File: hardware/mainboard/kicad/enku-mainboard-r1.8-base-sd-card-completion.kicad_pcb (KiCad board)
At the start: 4 copper layers, 59 x 101 mm, 132 parts, among them J1 1S LiPo + NTC, J2 Hirose DM3AT-SF-PEJM5, J3 FH34SRJ-24S-0.5SH(50), J5 GCT USB4105-GF-A-120, J6 4-pin pogo dock, J7 Tag-Connect TC2030-IDC-NL, Q1 IRLML6346TRPBF, Q2 AO3401A, SW1 HARD POWER, SW2 BOOT / RECOVERY, SW3 BTN_L1, SW4 BTN_L2, SW5 BTN_R1, SW6 BTN_R2, U1 ESP32-S3-WROOM-1-N16R8, U10 TLV3012BIDBVR, U2 TPS2121, U3 BQ25185DLHR, U4 TPS63802DLAR, U5 BMI270, U8 USBLC6-2SC6, U9 TMUX1101DBVR

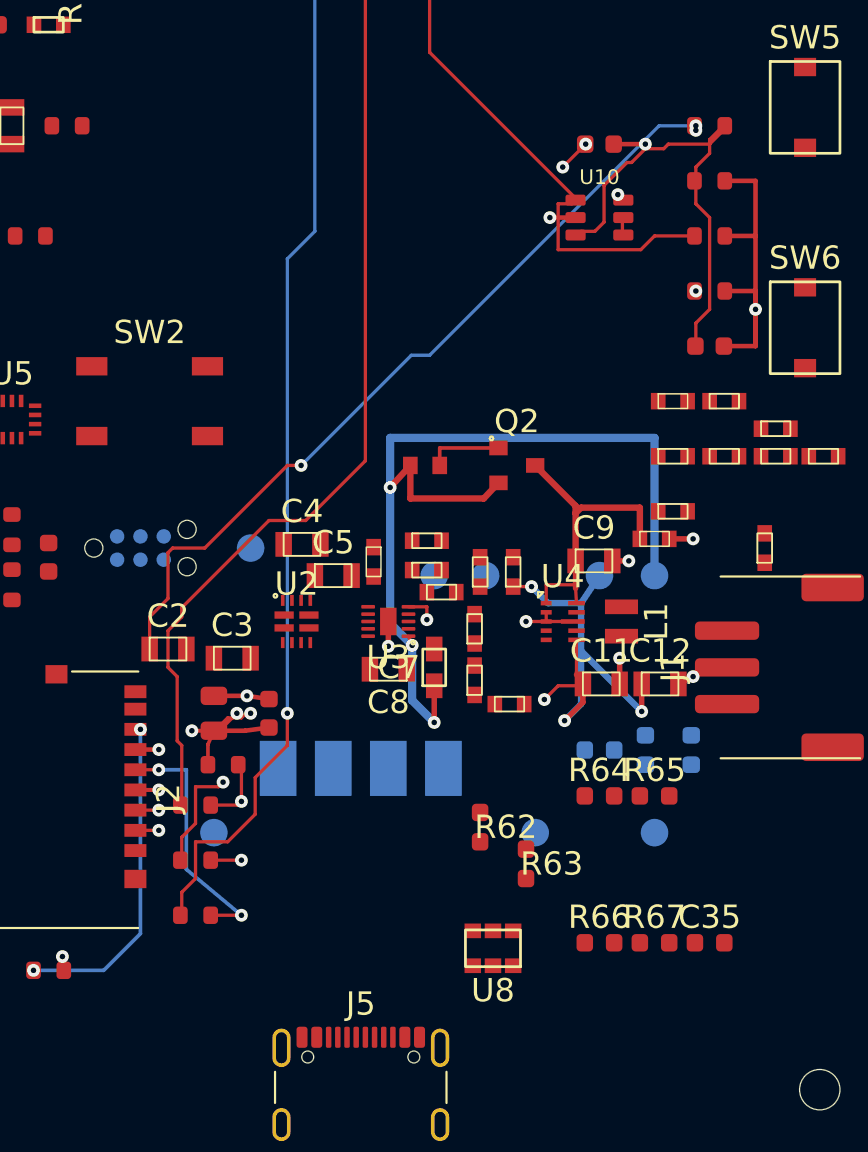
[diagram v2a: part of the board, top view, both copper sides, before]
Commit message: R41: correct ST ESD lands and route USB CC/VBUS power; fix GND clearances
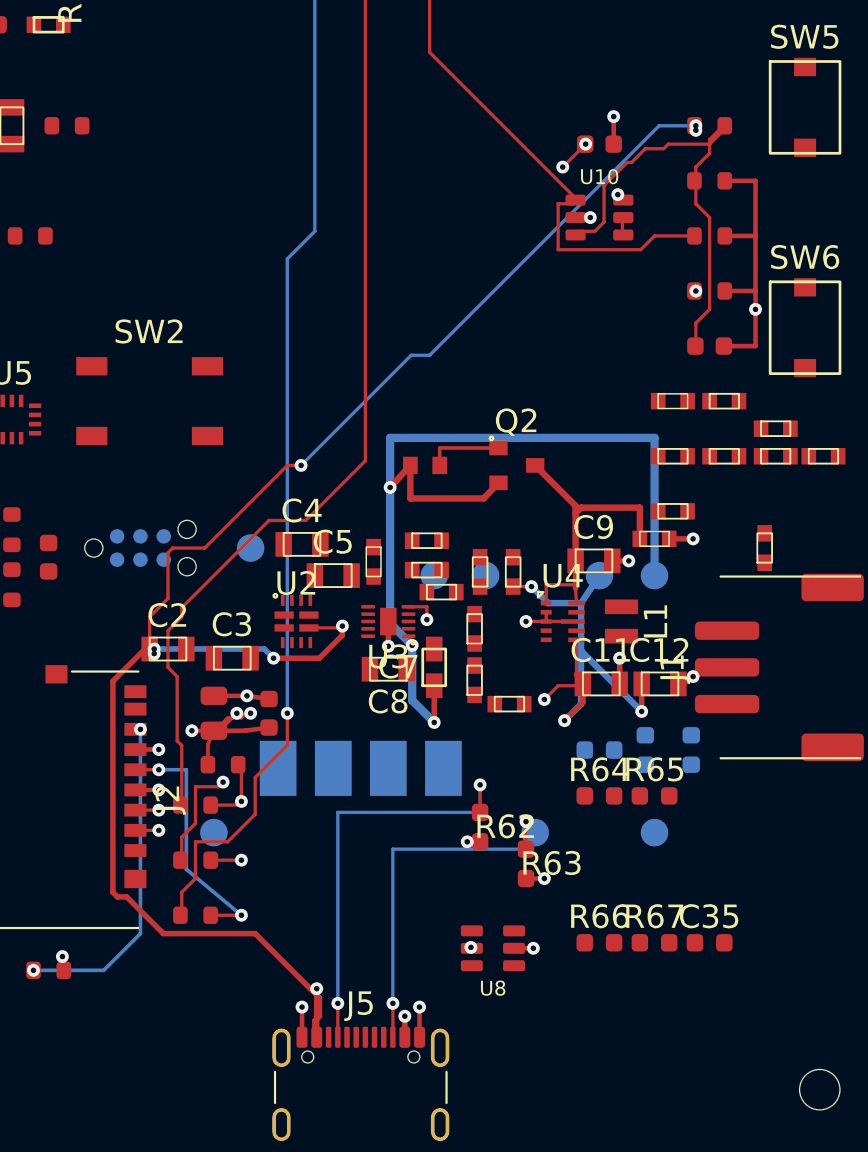
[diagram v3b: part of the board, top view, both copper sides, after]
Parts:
- U8: footprint Package_TO_SOT_SMD:SOT-23-6 -> ENKU:USBLC6_2SC6_ST_SOT23_6L
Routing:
- net VBUS_USB: track 53.0 -> 134.0 mm, vias 4 -> 11
- net USB_CC1: track 0.00 -> 23.0 mm, vias 0 -> 2
- net USB_CC2: track 0.00 -> 20.5 mm, vias 0 -> 2
- net GND: track 43.0 -> 45.2 mm, vias 15 -> 20
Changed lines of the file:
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@@
     (pad "S" thru_hole oval (at 4.32 1.075) (size 1 1.8) (drill oval 0.6 1.4) (layers "*.Cu" "*.Mask") (net 8 "USB_SHIELD"))
   )
-  (footprint "Package_TO_SOT_SMD:SOT-23-6" (layer "F.Cu")
-    (at 54.2 108.8 180)
-    (property "Reference" "U8" (at 0 -2.3 0) (layer "F.SilkS"))
-    (property "Value" "USBLC6-2SC6" (at 0 2.3 0) (layer "F.Fab") hide)
-    (fp_rect (start -1.5 -1) (end 1.5 1)
-      (stroke (width 0.15) (type default)) (fill none) (layer "F.SilkS"))
-    (pad "1" smd rect (at -1.1 -0.95) (size 0.9 0.8) (layers "F.Cu" "F.Paste" "F.Mask") (net 6 "USB_DP_CONN"))
-    (pad "2" smd rect (at 0 -0.95) (size 0.9 0.8) (layers "F.Cu" "F.Paste" "F.Mask") (net 1 "GND"))
-    (pad "3" smd rect (at 1.1 -0.95) (size 0.9 0.8) (layers "F.Cu" "F.Paste" "F.Mask") (net 7 "USB_DM_CONN"))
-    (pad "4" smd rect (at 1.1 0.95) (size 0.9 0.8) (layers "F.Cu" "F.Paste" "F.Mask") (net 7 "USB_DM_CONN"))
-    (pad "5" smd rect (at 0 0.95) (size 0.9 0.8) (layers "F.Cu" "F.Paste" "F.Mask") (net 3 "VBUS_USB"))
-    (pad "6" smd rect (at -1.1 0.95) (size 0.9 0.8) (layers "F.Cu" "F.Paste" "F.Mask") (net 6 "USB_DP_CONN"))
-  )
+  (footprint "ENKU:USBLC6_2SC6_ST_SOT23_6L" (layer "F.Cu") (at 54.2 108.8 180) (attr smd)
+(property "Reference" "U8" (at 0 -2.2) (layer "F.SilkS") (effects (font (size 0.8 0.8) (thickness 0.12))))
+(property "Value" "USBLC6-2SC6" (at 0 2.2) (layer "F.Fab") (effects (font (size 0.8 0.8) (thickness 0.12))))
+(fp_rect (start -0.8 -1.5) (end 0.8 1.5) (stroke (width 0.1) (type default)) (fill none) (layer "F.Fab"))
+(fp_rect (start -2 -1.75) (end 2 1.75) (stroke (width 0.05) (type default)) (fill none) (layer "F.CrtYd"))
+(pad "1" smd roundrect (at -1.15 -0.95) (size 1.2 0.6) (layers "F.Cu" "F.Paste" "F.Mask") (roundrect_rratio 0.2) (net 6 "USB_DP_CONN"))
+(pad "2" smd roundrect (at -1.15 0) (size 1.2 0.6) (layers "F.Cu" "F.Paste" "F.Mask") (roundrect_rratio 0.2) (net 1 "GND"))
+(pad "3" smd roundrect (at -1.15 0.95) (size 1.2 0.6) (layers "F.Cu" "F.Paste" "F.Mask") (roundrect_rratio 0.2) (net 7 "USB_DM_CONN"))
+(pad "4" smd roundrect (at 1.15 0.95) (size 1.2 0.6) (layers "F.Cu" "F.Paste" "F.Mask") (roundrect_rratio 0.2) (net 7 "USB_DM_CONN"))
+(pad "5" smd roundrect (at 1.15 0) (size 1.2 0.6) (layers "F.Cu" "F.Paste" "F.Mask") (roundrect_rratio 0.2) (net 3 "VBUS_USB"))
+(pad "6" smd roundrect (at 1.15 -0.95) (size 1.2 0.6) (layers "F.Cu" "F.Paste" "F.Mask") (roundrect_rratio 0.2) (net 6 "USB_DP_CONN"))
+)
   (footprint "ENKU:HARD_POWER_SWITCH_PLACEMENT" (layer "F.Cu")
     (at 30.5 29)
@@
     (min_thickness 0.25)
     (fill yes (thermal_gap 0.30) (thermal_bridge_width 0.30))
-    (polygon (pts (xy 27 35) (xy 69 35) (xy 69 111) (xy 27 111)))
+    (polygon (pts (xy 27 35) (xy 69 35) (xy 69 119) (xy 27 119)))
   )
   (segment (start 39 95.05) (end 40.8 95.05) (width 0.25) (layer "F.Cu") (net 1))
@@
     (min_thickness 0.25)
     (fill yes (thermal_gap 0.30) (thermal_bridge_width 0.30))
-    (polygon (pts (xy 27 35) (xy 69 35) (xy 69 111) (xy 27 111)))
+    (polygon (pts (xy 27 35) (xy 69 35) (xy 69 119) (xy 27 119)))
   )
   (segment (start 27.74 53.75) (end 27.74 55.5) (width 0.25) (layer "F.Cu") (net 1))
@@
   (segment (start 35.46 46.5) (end 35.46 49.5) (width 0.25) (layer "F.Cu") (net 1))
   (segment (start 34.725 97.975) (end 36 97.975) (width 0.25) (layer "F.Cu") (net 1))
-  (segment (start 58.7 69) (end 57.3 69) (width 0.25) (layer "F.Cu") (net 1))
-  (segment (start 60.775 65) (end 62.5 65) (width 0.25) (layer "F.Cu") (net 1))
+  (segment (start 58.7 69) (end 59.5 69) (width 0.25) (layer "F.Cu") (net 1))
+  (segment (start 60.775 65) (end 60.775 63.5) (width 0.25) (layer "F.Cu") (net 1))
   (segment (start 66.825 67) (end 68.5 67) (width 0.25) (layer "F.Cu") (net 1))
   (segment (start 68.5 67) (end 68.5 70) (width 0.25) (layer "F.Cu") (net 1))
@@
   (segment (start 68.5 70) (end 68.5 73) (width 0.25) (layer "F.Cu") (net 1))
   (segment (start 68.5 73) (end 66.825 73) (width 0.25) (layer "F.Cu") (net 1))
-  (segment (start 68.5 73) (end 68.5 76) (width 0.25) (layer "F.Cu") (net 1))
   (segment (start 68.5 76) (end 66.775 76) (width 0.25) (layer "F.Cu") (net 1))
   (segment (start 68.5 73) (end 68.5 74) (width 0.25) (layer "F.Cu") (net 1))
@@
   (via (at 35.46 49.5) (size 0.70) (drill 0.30) (layers "F.Cu" "B.Cu") (net 1))
   (via (at 36 97.975) (size 0.70) (drill 0.30) (layers "F.Cu" "B.Cu") (net 1))
-  (via (at 57.3 69) (size 0.70) (drill 0.30) (layers "F.Cu" "B.Cu") (net 1))
-  (via (at 62.5 65) (size 0.70) (drill 0.30) (layers "F.Cu" "B.Cu") (net 1))
+  (via (at 59.5 69) (size 0.70) (drill 0.30) (layers "F.Cu" "B.Cu") (net 1))
+  (via (at 60.775 63.5) (size 0.70) (drill 0.30) (layers "F.Cu" "B.Cu") (net 1))
   (via (at 68.5 74) (size 0.70) (drill 0.30) (layers "F.Cu" "B.Cu") (net 1))
+  (segment (start 45.75 113.645) (end 45.75 111.8) (width 0.18) (layer "F.Cu") (net 4))
+  (segment (start 45.75 111.8) (end 45.75 101.4) (width 0.18) (layer "B.Cu") (net 4))
+  (segment (start 45.75 101.4) (end 53.5 101.4) (width 0.18) (layer "B.Cu") (net 4))
+  (segment (start 53.5 101.4) (end 53.5 99.9) (width 0.18) (layer "B.Cu") (net 4))
+  (segment (start 53.5 99.9) (end 53.5 101.4) (width 0.18) (layer "F.Cu") (net 4))
+  (segment (start 48.75 113.645) (end 48.75 111.8) (width 0.18) (layer "F.Cu") (net 5))
+  (segment (start 48.75 111.8) (end 48.75 103.4) (width 0.18) (layer "B.Cu") (net 5))
+  (segment (start 48.75 103.4) (end 56 103.4) (width 0.18) (layer "B.Cu") (net 5))
+  (segment (start 56 103.4) (end 56 101.9) (width 0.18) (layer "B.Cu") (net 5))
+  (segment (start 56 101.9) (end 56 103.4) (width 0.18) (layer "F.Cu") (net 5))
+  (segment (start 43.8 113.645) (end 43.8 112.0) (width 0.25) (layer "F.Cu") (net 1))
+  (segment (start 50.2 113.645) (end 50.2 112.0) (width 0.25) (layer "F.Cu") (net 1))
+  (segment (start 53.5 103) (end 52.8 103) (width 0.25) (layer "F.Cu") (net 1))
+  (segment (start 56 105) (end 57 105) (width 0.25) (layer "F.Cu") (net 1))
+  (segment (start 55.35 108.8) (end 56.4 108.8) (width 0.25) (layer "F.Cu") (net 1))
+  (via (at 45.75 111.8) (size 0.70) (drill 0.30) (layers "F.Cu" "B.Cu") (net 4))
+  (via (at 53.5 99.9) (size 0.70) (drill 0.30) (layers "F.Cu" "B.Cu") (net 4))
+  (via (at 48.75 111.8) (size 0.70) (drill 0.30) (layers "F.Cu" "B.Cu") (net 5))
+  (via (at 56 101.9) (size 0.70) (drill 0.30) (layers "F.Cu" "B.Cu") (net 5))
+  (via (at 43.8 112.0) (size 0.70) (drill 0.30) (layers "F.Cu" "B.Cu") (net 1))
+  (via (at 50.2 112.0) (size 0.70) (drill 0.30) (layers "F.Cu" "B.Cu") (net 1))
+  (via (at 52.8 103) (size 0.70) (drill 0.30) (layers "F.Cu" "B.Cu") (net 1))
+  (via (at 57 105) (size 0.70) (drill 0.30) (layers "F.Cu" "B.Cu") (net 1))
+  (via (at 56.4 108.8) (size 0.70) (drill 0.30) (layers "F.Cu" "B.Cu") (net 1))
+  (segment (start 44.175 91.35) (end 46 91.35) (width 0.18) (layer "F.Cu") (net 3))
+  (segment (start 46 91.35) (end 46 91.25) (width 0.18) (layer "F.Cu") (net 3))
+  (via (at 46 91.25) (size 0.70) (drill 0.30) (layers "F.Cu" "B.Cu") (net 3))
+  (segment (start 49.4 113.645) (end 49.4 112.5) (width 0.30) (layer "F.Cu") (net 3))
+  (segment (start 44.6 113.645) (end 44.6 111) (width 0.30) (layer "F.Cu") (net 3))
+  (segment (start 49.4 112.5) (end 44.6 112.5) (width 0.30) (layer "In1.Cu") (net 3))
+  (segment (start 44.6 112.5) (end 44.6 111) (width 0.30) (layer "In1.Cu") (net 3))
+  (via (at 49.4 112.5) (size 0.70) (drill 0.30) (layers "F.Cu" "B.Cu") (net 3))
+  (via (at 44.6 111) (size 0.70) (drill 0.30) (layers "F.Cu" "B.Cu") (net 3))
+  (segment (start 44.5 113.75) (end 44.5 112.75) (width 0.30) (layer "F.Cu") (net 3))
+  (segment (start 44.5 112.75) (end 44.75 112.5) (width 0.30) (layer "F.Cu") (net 3))
+  (segment (start 44.75 112.5) (end 44.75 111.5) (width 0.30) (layer "F.Cu") (net 3))
+  (segment (start 44.75 111.5) (end 41.25 108.0) (width 0.30) (layer "F.Cu") (net 3))
+  (segment (start 41.25 108.0) (end 36.25 108.0) (width 0.30) (layer "F.Cu") (net 3))
+  (segment (start 36.25 108.0) (end 34.25 106.0) (width 0.30) (layer "F.Cu") (net 3))
+  (segment (start 34.25 106.0) (end 33.75 106.0) (width 0.30) (layer "F.Cu") (net 3))
+  (segment (start 33.75 106.0) (end 33.5 105.75) (width 0.30) (layer "F.Cu") (net 3))
+  (segment (start 33.5 105.75) (end 33.5 94.25) (width 0.30) (layer "F.Cu") (net 3))
+  (segment (start 33.5 94.25) (end 35.25 92.5) (width 0.30) (layer "F.Cu") (net 3))
+  (segment (start 35.25 92.5) (end 35.5 92.5) (width 0.30) (layer "F.Cu") (net 3))
+  (segment (start 35.5 92.5) (end 35.75 92.5) (width 0.30) (layer "F.Cu") (net 3))
+  (segment (start 35.75 92.5) (end 41.75 92.5) (width 0.30) (layer "B.Cu") (net 3))
+  (segment (start 41.75 92.5) (end 42.25 93.0) (width 0.30) (layer "B.Cu") (net 3))
+  (segment (start 42.25 93.0) (end 44.75 93.0) (width 0.30) (layer "F.Cu") (net 3))
+  (segment (start 44.75 93.0) (end 46.0 91.75) (width 0.30) (layer "F.Cu") (net 3))
+  (segment (start 46.0 91.75) (end 46.0 91.25) (width 0.30) (layer "F.Cu") (net 3))
+  (via (at 35.75 92.5) (size 0.70) (drill 0.30) (layers "F.Cu" "B.Cu") (net 3))
+  (via (at 42.25 93.0) (size 0.70) (drill 0.30) (layers "F.Cu" "B.Cu") (net 3))
+  (segment (start 35.5 92.5) (end 35.75 92.75) (width 0.30) (layer "F.Cu") (net 3))
+  (segment (start 35.75 92.75) (end 38.75 95.75) (width 0.30) (layer "In1.Cu") (net 3))
+  (segment (start 38.75 95.75) (end 38.75 100.5) (width 0.30) (layer "In1.Cu") (net 3))
+  (segment (start 38.75 100.5) (end 45.25 107.0) (width 0.30) (layer "In1.Cu") (net 3))
+  (segment (start 45.25 107.0) (end 51.25 107.0) (width 0.30) (layer "In1.Cu") (net 3))
+  (segment (start 51.25 107.0) (end 53.0 108.75) (width 0.30) (layer "In1.Cu") (net 3))
+  (via (at 35.75 92.75) (size 0.70) (drill 0.30) (layers "F.Cu" "B.Cu") (net 3))
+  (via (at 53.0 108.75) (size 0.70) (drill 0.30) (layers "F.Cu" "B.Cu") (net 3))
 )

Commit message: R41: clear CC2 dock test pad; consolidate VBUS vias and archive Native diagnostics
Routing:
- net USB_CC2: track 20.5 -> 19.9 mm
- net VBUS_USB: track 134.0 -> 134.1 mm, vias 11 -> 8
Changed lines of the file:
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@@
   (via (at 43.75 82.5) (size 0.70) (drill 0.30) (layers "F.Cu" "B.Cu") (net 3))
   (via (at 65.25 64.0) (size 0.70) (drill 0.30) (layers "F.Cu" "B.Cu") (net 3))
-  (segment (start 65.25 64.0) (end 65.25 64.25) (width 0.18) (layer "F.Cu") (net 3))
-  (segment (start 65.25 64.25) (end 65.25 73.0) (width 0.18) (layer "In1.Cu") (net 3))
-  (via (at 65.25 64.25) (size 0.70) (drill 0.30) (layers "F.Cu" "B.Cu") (net 3))
+  (segment (start 65.25 64.0) (end 65.25 73.0) (width 0.18) (layer "In1.Cu") (net 3))
   (via (at 65.25 73.0) (size 0.70) (drill 0.30) (layers "F.Cu" "B.Cu") (net 3))
   (zone (net 1) (net_name "GND") (layer "In1.Cu") (hatch edge 0.5)
@@
   (segment (start 53.5 99.9) (end 53.5 101.4) (width 0.18) (layer "F.Cu") (net 4))
   (segment (start 48.75 113.645) (end 48.75 111.8) (width 0.18) (layer "F.Cu") (net 5))
-  (segment (start 48.75 111.8) (end 48.75 103.4) (width 0.18) (layer "B.Cu") (net 5))
-  (segment (start 48.75 103.4) (end 56 103.4) (width 0.18) (layer "B.Cu") (net 5))
-  (segment (start 56 103.4) (end 56 101.9) (width 0.18) (layer "B.Cu") (net 5))
-  (segment (start 56 101.9) (end 56 103.4) (width 0.18) (layer "F.Cu") (net 5))
+  (segment (start 48.75 111.8) (end 48.75 106.4) (width 0.18) (layer "B.Cu") (net 5))
+  (segment (start 48.75 106.4) (end 56 106.4) (width 0.18) (layer "B.Cu") (net 5))
+  (segment (start 56 106.4) (end 54.8 106.4) (width 0.18) (layer "B.Cu") (net 5))
+  (segment (start 54.8 106.4) (end 54.8 103.4) (width 0.18) (layer "F.Cu") (net 5))
   (segment (start 43.8 113.645) (end 43.8 112.0) (width 0.25) (layer "F.Cu") (net 1))
   (segment (start 50.2 113.645) (end 50.2 112.0) (width 0.25) (layer "F.Cu") (net 1))
@@
   (via (at 53.5 99.9) (size 0.70) (drill 0.30) (layers "F.Cu" "B.Cu") (net 4))
   (via (at 48.75 111.8) (size 0.70) (drill 0.30) (layers "F.Cu" "B.Cu") (net 5))
-  (via (at 56 101.9) (size 0.70) (drill 0.30) (layers "F.Cu" "B.Cu") (net 5))
+  (via (at 54.8 106.4) (size 0.70) (drill 0.30) (layers "F.Cu" "B.Cu") (net 5))
   (via (at 43.8 112.0) (size 0.70) (drill 0.30) (layers "F.Cu" "B.Cu") (net 1))
   (via (at 50.2 112.0) (size 0.70) (drill 0.30) (layers "F.Cu" "B.Cu") (net 1))
@@
   (segment (start 44.175 91.35) (end 46 91.35) (width 0.18) (layer "F.Cu") (net 3))
   (segment (start 46 91.35) (end 46 91.25) (width 0.18) (layer "F.Cu") (net 3))
-  (via (at 46 91.25) (size 0.70) (drill 0.30) (layers "F.Cu" "B.Cu") (net 3))
   (segment (start 49.4 113.645) (end 49.4 112.5) (width 0.30) (layer "F.Cu") (net 3))
   (segment (start 44.6 113.645) (end 44.6 111) (width 0.30) (layer "F.Cu") (net 3))
@@
   (via (at 35.75 92.5) (size 0.70) (drill 0.30) (layers "F.Cu" "B.Cu") (net 3))
   (via (at 42.25 93.0) (size 0.70) (drill 0.30) (layers "F.Cu" "B.Cu") (net 3))
-  (segment (start 35.5 92.5) (end 35.75 92.75) (width 0.30) (layer "F.Cu") (net 3))
-  (segment (start 35.75 92.75) (end 38.75 95.75) (width 0.30) (layer "In1.Cu") (net 3))
+  (segment (start 35.5 92.5) (end 35.75 92.5) (width 0.30) (layer "F.Cu") (net 3))
+  (segment (start 35.75 92.5) (end 38.75 95.75) (width 0.30) (layer "In1.Cu") (net 3))
   (segment (start 38.75 95.75) (end 38.75 100.5) (width 0.30) (layer "In1.Cu") (net 3))
   (segment (start 38.75 100.5) (end 45.25 107.0) (width 0.30) (layer "In1.Cu") (net 3))
   (segment (start 45.25 107.0) (end 51.25 107.0) (width 0.30) (layer "In1.Cu") (net 3))
   (segment (start 51.25 107.0) (end 53.0 108.75) (width 0.30) (layer "In1.Cu") (net 3))
-  (via (at 35.75 92.75) (size 0.70) (drill 0.30) (layers "F.Cu" "B.Cu") (net 3))
   (via (at 53.0 108.75) (size 0.70) (drill 0.30) (layers "F.Cu" "B.Cu") (net 3))
+  (segment (start 54.8 103.4) (end 56 103.4) (width 0.18) (layer "F.Cu") (net 5))
 )
